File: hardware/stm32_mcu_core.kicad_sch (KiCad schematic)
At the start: 27 parts, among them J4 RGB LED Ring, U6 SN74LVC1G126DBVR, U7 STM32G431KBTx, U8 SN74LVC1G125DBVR, U9 SN74AHCT1G125DBVR

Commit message: remove rgb led capactiors
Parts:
- C29, C30: now not fitted
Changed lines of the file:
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@@
 		(on_board yes)
 		(in_pos_files yes)
-		(dnp no)
+		(dnp yes)
 		(fields_autoplaced yes)
 		(property "Reference" "#PWR058"
@@
 		(on_board yes)
 		(in_pos_files yes)
-		(dnp no)
+		(dnp yes)
 		(fields_autoplaced yes)
 		(property "Reference" "#PWR059"
@@
 		(on_board yes)
 		(in_pos_files yes)
-		(dnp no)
+		(dnp yes)
 		(fields_autoplaced yes)
 		(property "Reference" "C30"
@@
 		(on_board yes)
 		(in_pos_files yes)
-		(dnp no)
+		(dnp yes)
 		(fields_autoplaced yes)
 		(property "Reference" "C29"
@@
 		(on_board yes)
 		(in_pos_files yes)
-		(dnp no)
+		(dnp yes)
 		(fields_autoplaced yes)
 		(property "Reference" "#PWR066"
@@
 		(on_board yes)
 		(in_pos_files yes)
-		(dnp no)
+		(dnp yes)
 		(fields_autoplaced yes)
 		(property "Reference" "#PWR065"

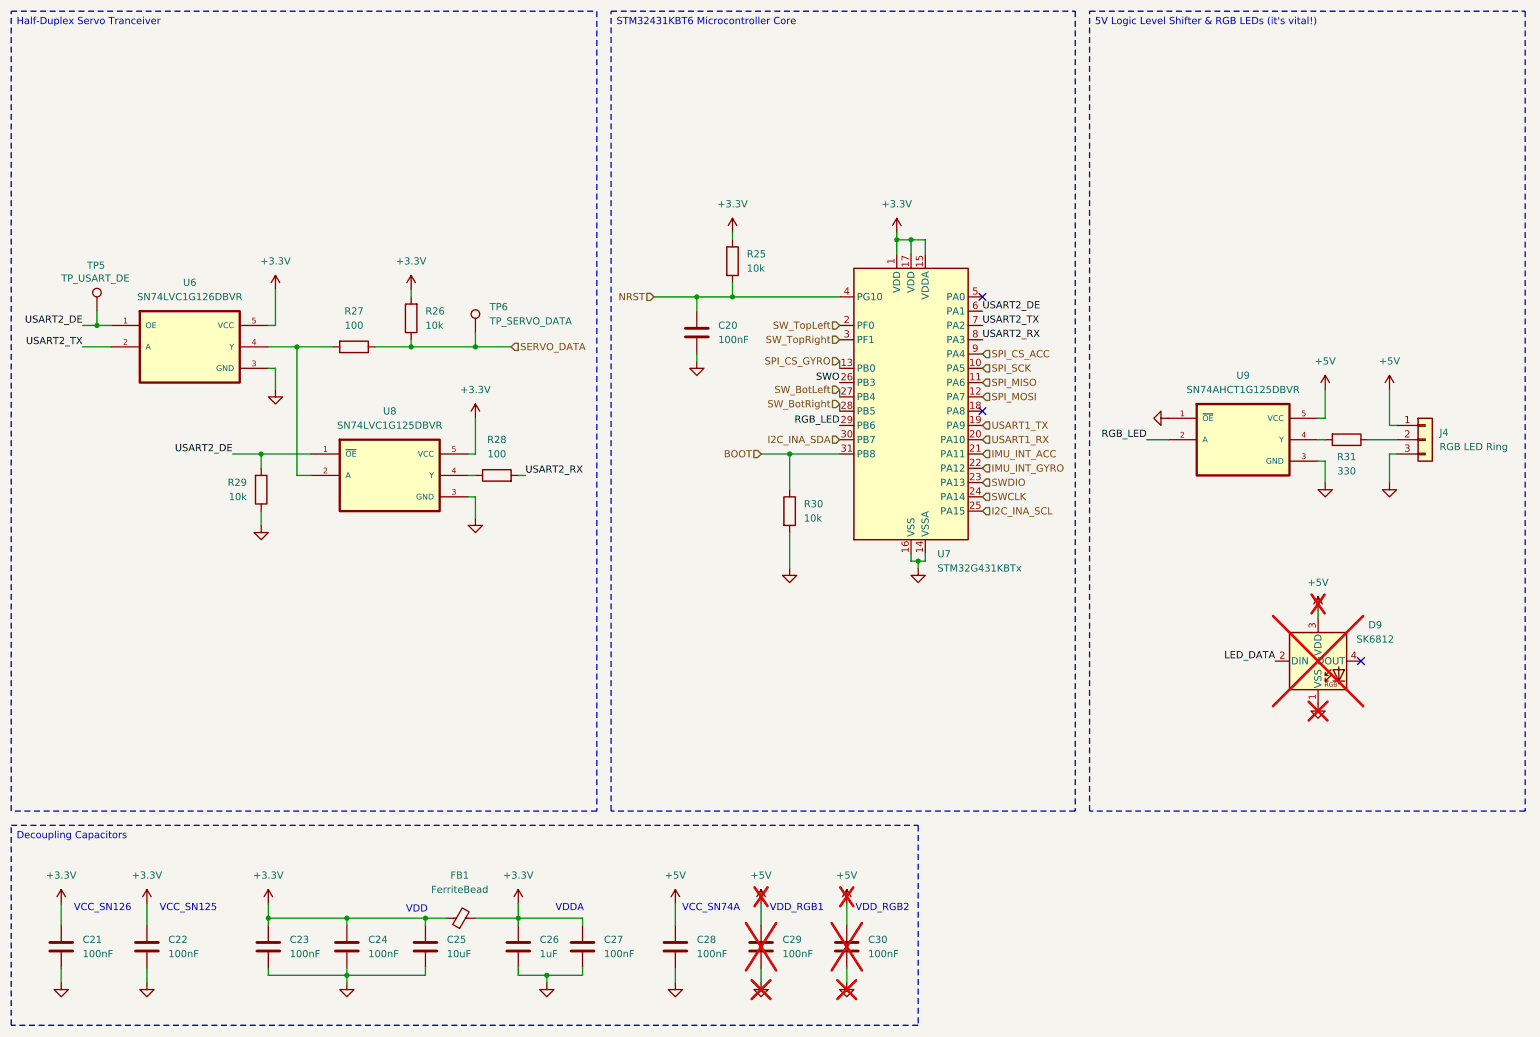
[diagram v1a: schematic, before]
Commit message: replacing components
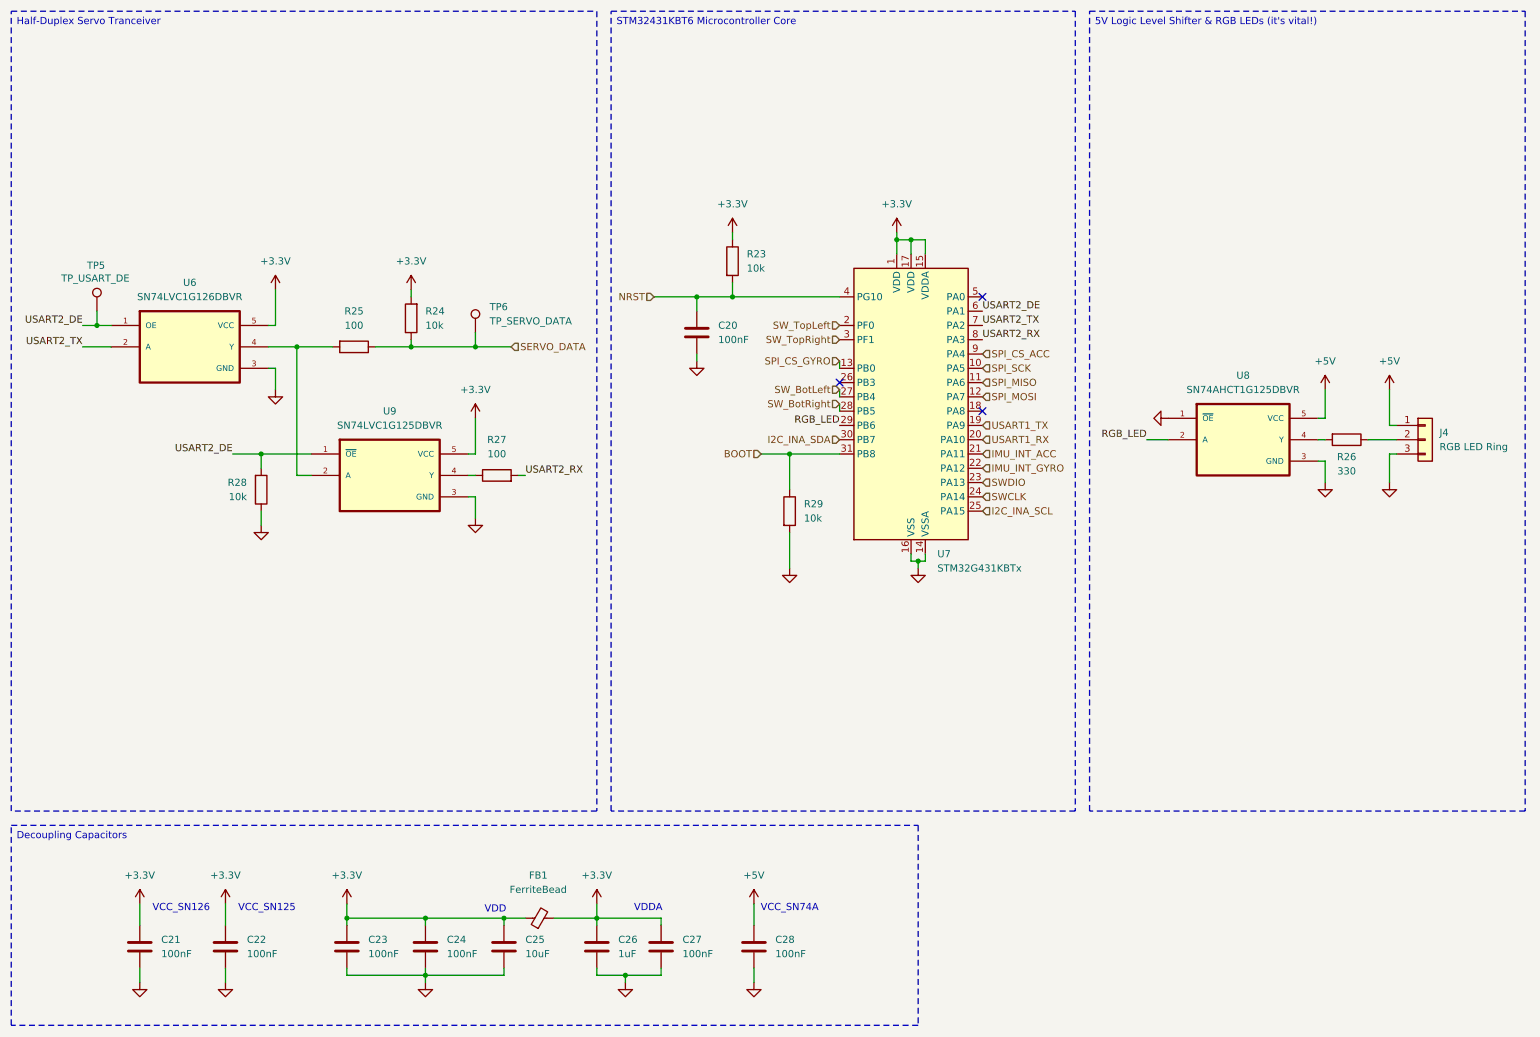
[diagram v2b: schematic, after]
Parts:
- removed C29, C30: 100nF, Capacitor_SMD:C_0402_1005Metric, symbol Device:C
- removed D9: SK6812, LED_SMD:LED_SK6812_EC15_1.5x1.5mm, symbol LED:SK6812
- renumbered R25 to R23, R26 to R24, R27 to R25, R31 to R26, R28 to R27, R29 to R28, R30 to R29, U9 to U8, U8 to U9
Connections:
- net SWO: no longer names the net of U7.26 (PB3)
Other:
- note removed: "VDD_RGB1"
- note removed: "VDD_RGB2"
- moved on the sheet: C21, C22, C23, C24, C25, C26, C27, C28, FB1

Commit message: schematic update
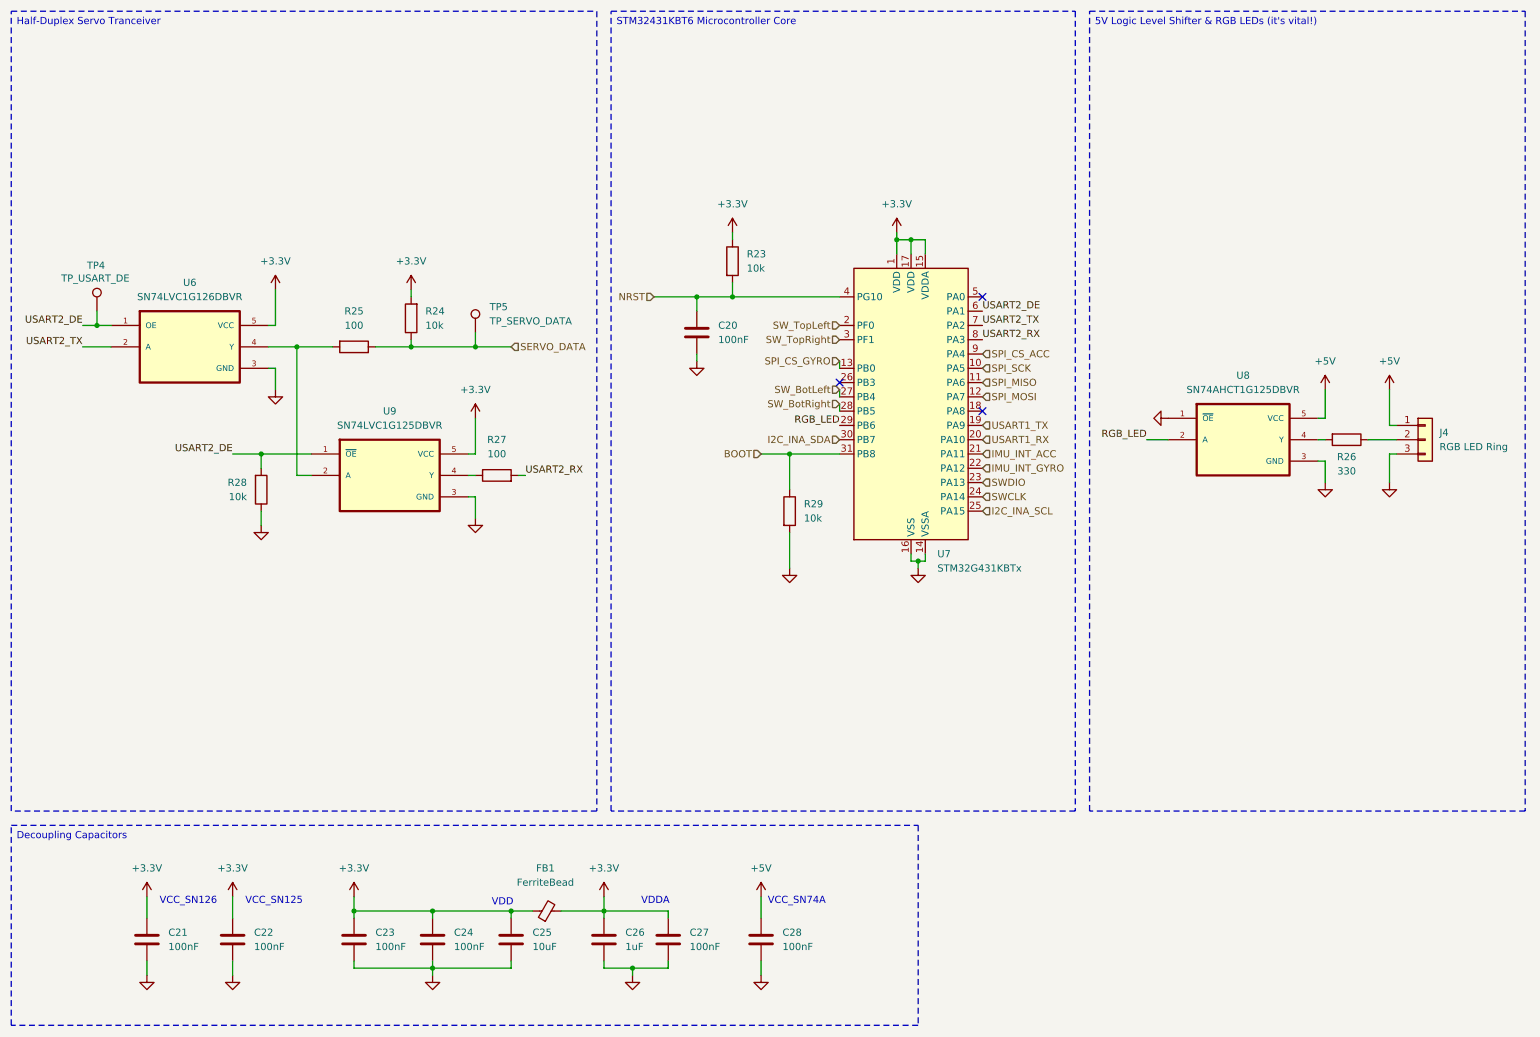
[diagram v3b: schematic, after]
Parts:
- renumbered TP5 to TP4, TP6 to TP5
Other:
- moved on the sheet: C21, C22, C23, C24, C25, C26, C27, C28, FB1

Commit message: update schematic
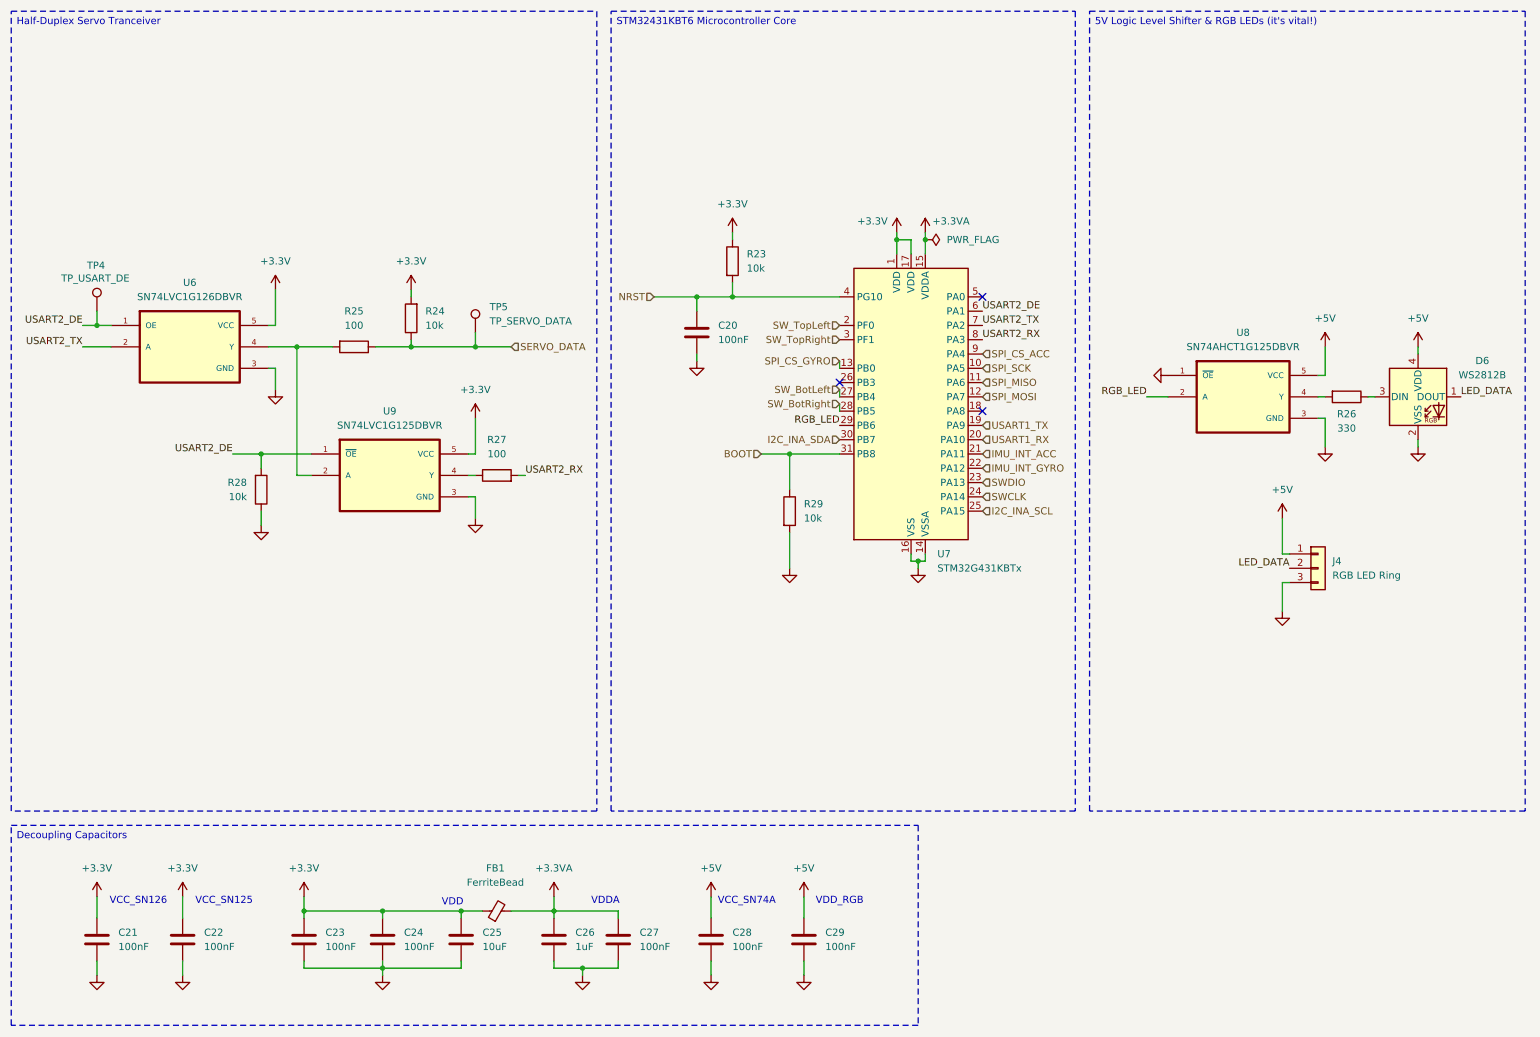
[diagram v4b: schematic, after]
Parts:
- added C29: 100nF, Capacitor_SMD:C_0402_1005Metric, symbol Device:C
- added D6: WS2812B, LED_SMD:LED_WS2812B-2020_PLCC4_2.0x2.0mm, symbol LED:WS2812B-2020
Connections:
- net +3.3V: no longer C26.1, C27.1, FB1.2, U7.15 (VDDA)
- net +5V: now also C29.1, D6.4 (VDD)
- net GND: now also C29.2, D6.2 (VSS)
- net at R26.1: now also D6.3 (DIN); no longer J4.2 (Pin_2)
- new net +3.3VA: C26.1, C27.1, FB1.2, U7.15 (VDDA)
- new net LED_DATA: D6.1 (DOUT), J4.2 (Pin_2)
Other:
- note added: "VDD_RGB"
- moved on the sheet: C21, C22, C23, C24, C25, C26, C27, C28, FB1, R26, U8

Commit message: ready for production
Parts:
- D6: JLCPCB Part # (none) -> C965555; MPN (none) -> WS2812B-2020
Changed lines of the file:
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@@
 			)
 		)
-		(property "MANUFACTURER" ""
-			(at 44.45 180.34 0)
-			(hide yes)
-			(show_name no)
-			(do_not_autoplace no)
-			(effects
-				(font
-					(size 1.27 1.27)
-				)
-			)
-		)
 		(property "MP" ""
 			(at 44.45 180.34 0)
@@
 			)
 		)
-		(property "MANUFACTURER" ""
-			(at 100.33 97.79 90)
-			(hide yes)
-			(show_name no)
-			(do_not_autoplace no)
-			(effects
-				(font
-					(size 1.27 1.27)
-				)
-			)
-		)
 		(property "MP" ""
 			(at 100.33 97.79 90)
@@
 			)
 		)
-		(property "MANUFACTURER" ""
-			(at 29.21 180.34 0)
-			(hide yes)
-			(show_name no)
-			(do_not_autoplace no)
-			(effects
-				(font
-					(size 1.27 1.27)
-				)
-			)
-		)
 		(property "MP" ""
 			(at 29.21 180.34 0)
@@
 			)
 		)
-		(property "MANUFACTURER" ""
-			(at 121.92 180.34 0)
-			(hide yes)
-			(show_name no)
-			(do_not_autoplace no)
-			(effects
-				(font
-					(size 1.27 1.27)
-				)
-			)
-		)
 		(property "MP" ""
 			(at 121.92 180.34 0)
@@
 			)
 		)
-		(property "MANUFACTURER" ""
-			(at 74.93 74.93 90)
-			(hide yes)
-			(show_name no)
-			(do_not_autoplace no)
-			(effects
-				(font
-					(size 1.27 1.27)
-				)
-			)
-		)
 		(property "MP" ""
 			(at 74.93 74.93 90)
@@
 			)
 		)
-		(property "MANUFACTURER" ""
-			(at 152.4 104.14 0)
-			(hide yes)
-			(show_name no)
-			(do_not_autoplace no)
-			(effects
-				(font
-					(size 1.27 1.27)
-				)
-			)
-		)
 		(property "MP" ""
 			(at 152.4 104.14 0)
@@
 			)
 		)
-		(property "MANUFACTURER" ""
-			(at 29.21 68.58 0)
-			(hide yes)
-			(show_name no)
-			(do_not_autoplace no)
-			(effects
-				(font
-					(size 1.27 1.27)
-				)
-			)
-		)
 		(property "MP" ""
 			(at 29.21 68.58 0)
@@
 			)
 		)
-		(property "MANUFACTURER" ""
-			(at 58.42 100.33 0)
-			(hide yes)
-			(show_name no)
-			(do_not_autoplace no)
-			(effects
-				(font
-					(size 1.27 1.27)
-				)
-			)
-		)
 		(property "MP" ""
 			(at 58.42 100.33 0)
@@
 			)
 		)
-		(property "MANUFACTURER" ""
-			(at 246.38 114.3 0)
-			(hide yes)
-			(show_name no)
-			(do_not_autoplace no)
-			(effects
-				(font
-					(size 1.27 1.27)
-				)
-			)
-		)
 		(property "MP" ""
 			(at 246.38 114.3 0)
@@
 			)
 		)
-		(property "MANUFACTURER" ""
-			(at 138.43 180.34 0)
-			(hide yes)
-			(show_name no)
-			(do_not_autoplace no)
-			(effects
-				(font
-					(size 1.27 1.27)
-				)
-			)
-		)
 		(property "MP" ""
 			(at 138.43 180.34 0)
@@
 			)
 		)
-		(property "MANUFACTURER" ""
-			(at 80.01 180.34 0)
-			(hide yes)
-			(show_name no)
-			(do_not_autoplace no)
-			(effects
-				(font
-					(size 1.27 1.27)
-				)
-			)
-		)
 		(property "MP" ""
 			(at 80.01 180.34 0)
@@
 			)
 		)
-		(property "MANUFACTURER" ""
-			(at 96.52 72.39 0)
-			(hide yes)
-			(show_name no)
-			(do_not_autoplace no)
-			(effects
-				(font
-					(size 1.27 1.27)
-				)
-			)
-		)
 		(property "MP" ""
 			(at 96.52 72.39 0)
@@
 			)
 		)
-		(property "MANUFACTURER" ""
-			(at 142.24 59.69 0)
-			(hide yes)
-			(show_name no)
-			(do_not_autoplace no)
-			(effects
-				(font
-					(size 1.27 1.27)
-				)
-			)
-		)
 		(property "MP" ""
 			(at 142.24 59.69 0)
@@
 			)
 		)
-		(property "MANUFACTURER" ""
-			(at 93.98 180.34 0)
-			(hide yes)
-			(show_name no)
-			(do_not_autoplace no)
-			(effects
-				(font
-					(size 1.27 1.27)
-				)
-			)
-		)
 		(property "MP" ""
 			(at 93.98 180.34 0)
@@
 			)
 		)
-		(property "MANUFACTURER" ""
-			(at 110.49 180.34 0)
-			(hide yes)
-			(show_name no)
-			(do_not_autoplace no)
-			(effects
-				(font
-					(size 1.27 1.27)
-				)
-			)
-		)
 		(property "MP" ""
 			(at 110.49 180.34 0)
@@
 			)
 		)
+		(property "MPN" "WS2812B-2020"
+			(at 264.16 83.82 0)
+			(hide yes)
+			(show_name no)
+			(do_not_autoplace no)
+			(effects
+				(font
+					(size 1.27 1.27)
+				)
+			)
+		)
+		(property "JLCPCB Part #" "C965555"
+			(at 264.16 83.82 0)
+			(hide yes)
+			(show_name no)
+			(do_not_autoplace no)
+			(effects
+				(font
+					(size 1.27 1.27)
+				)
+			)
+		)
 		(pin "3"
 		)
@@
 			)
 		)
-		(property "MANUFACTURER" ""
-			(at 100.33 175.26 90)
-			(hide yes)
-			(show_name no)
-			(do_not_autoplace no)
-			(effects
-				(font
-					(size 1.27 1.27)
-				)
-			)
-		)
 		(property "MP" ""
 			(at 100.33 175.26 90)
@@
 			)
 		)
-		(property "MANUFACTURER" ""
-			(at 85.09 69.85 0)
-			(hide yes)
-			(show_name no)
-			(do_not_autoplace no)
-			(effects
-				(font
-					(size 1.27 1.27)
-				)
-			)
-		)
 		(property "MP" ""
 			(at 85.09 69.85 0)
@@
 			)
 		)
-		(property "MANUFACTURER" ""
-			(at 135.89 72.39 0)
-			(hide yes)
-			(show_name no)
-			(do_not_autoplace no)
-			(effects
-				(font
-					(size 1.27 1.27)
-				)
-			)
-		)
 		(property "MP" ""
 			(at 135.89 72.39 0)
@@
 			)
 		)
-		(property "MANUFACTURER" ""
-			(at 251.46 83.82 90)
-			(hide yes)
-			(show_name no)
-			(do_not_autoplace no)
-			(effects
-				(font
-					(size 1.27 1.27)
-				)
-			)
-		)
 		(property "MP" ""
 			(at 251.46 83.82 90)
@@
 			)
 		)
-		(property "MANUFACTURER" ""
-			(at 154.94 180.34 0)
-			(hide yes)
-			(show_name no)
-			(do_not_autoplace no)
-			(effects
-				(font
-					(size 1.27 1.27)
-				)
-			)
-		)
 		(property "MP" ""
 			(at 154.94 180.34 0)
@@
 			(at 66.04 180.34 0)
 			(hide yes)
-			(show_name no)
-			(do_not_autoplace no)
-			(effects
-				(font
-					(size 1.27 1.27)
-				)
-			)
-		)
-		(property "MANUFACTURER" ""
-			(at 66.04 180.34 0)
-			(hide yes)

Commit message: release production files
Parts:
- R29: JLCPCB Part # (none) -> C60490; MPN CRCW040210K0JNED -> RC0402FR-0710KL
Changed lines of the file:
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@@
 			)
 		)
-		(property "MPN" "CRCW040210K0JNED"
+		(property "MPN" "RC0402FR-0710KL"
 			(at 152.4 104.14 0)
 			(hide yes)
@@
 			)
 		)
-		(property "JLCPCB Part #" ""
+		(property "JLCPCB Part #" "C60490"
 			(at 152.4 104.14 0)
 			(hide yes)
